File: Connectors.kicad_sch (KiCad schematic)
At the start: 18 parts, among them J1 Keystone 3579, J10 G-Switch-GT-USB-7025, J11 1.27mm 4 pin socket, J2 JST XH-S Balance Plug, J3 Keystone 3579, J4 Keystone 3569, J5 Keystone 3569, J6 Keystone 3579, J7 Keystone 3579, J8 Keystone 3569, J9 Keystone 3569

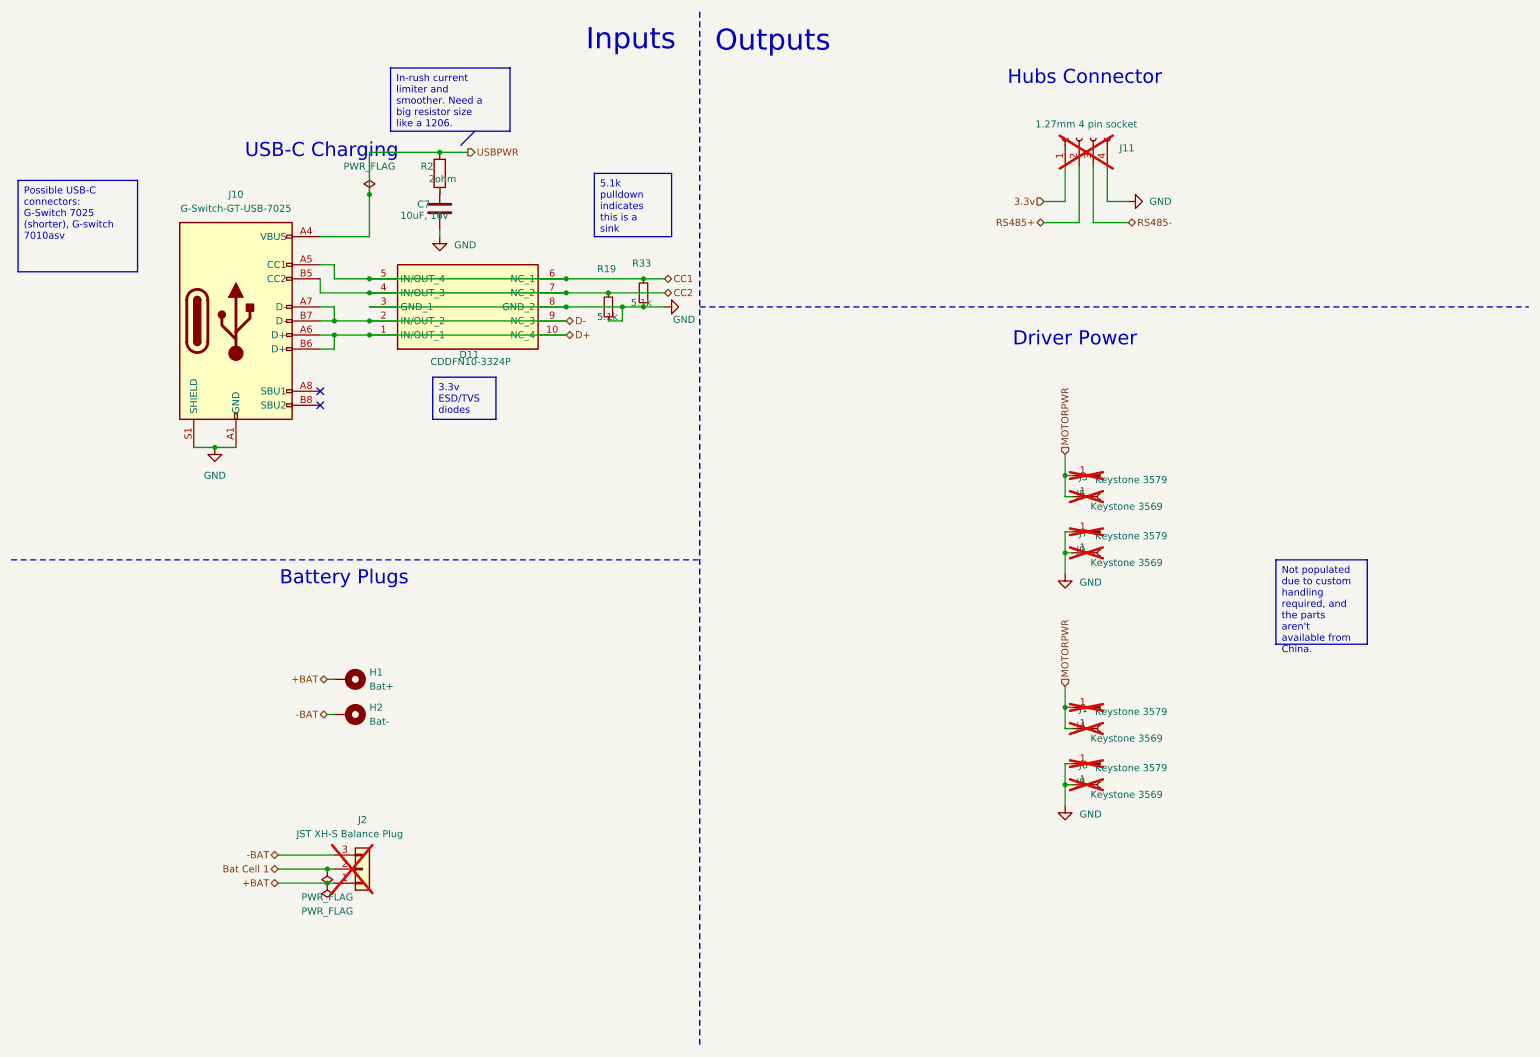
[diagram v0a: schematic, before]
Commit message: Updated to kicad 9
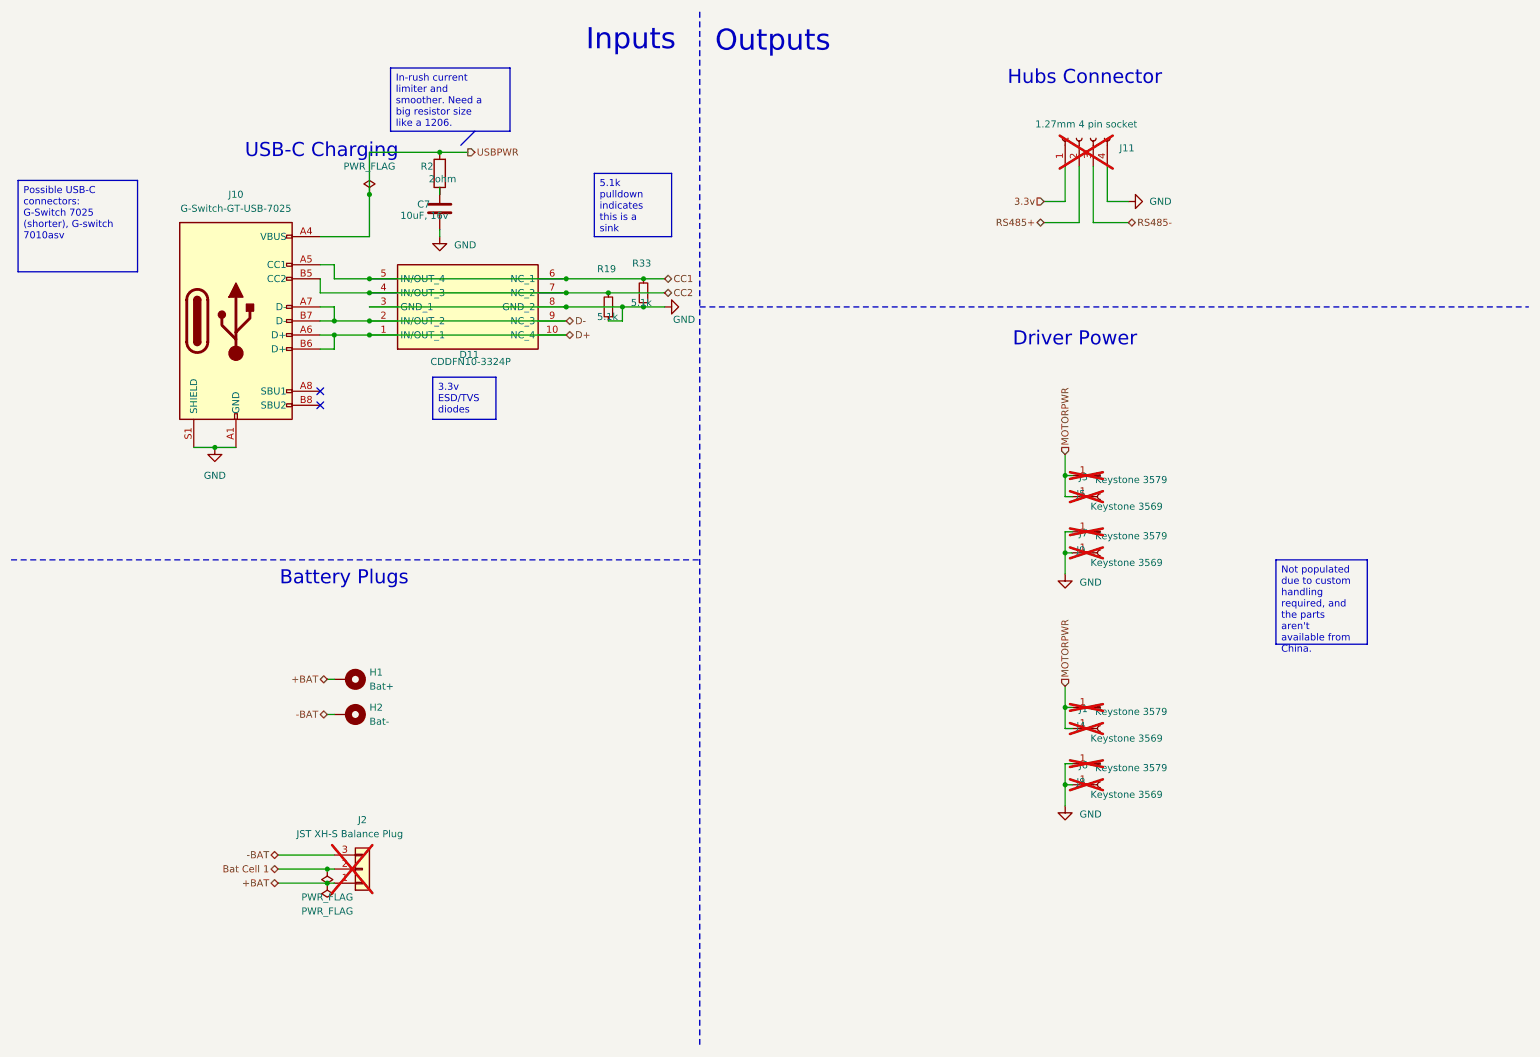
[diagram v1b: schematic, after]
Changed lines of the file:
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@@
 (kicad_sch
-	(version 20231120)
+	(version 20250114)
 	(generator "eeschema")
-	(generator_version "8.0")
+	(generator_version "9.0")
 	(paper "A4")
 	(title_block
 		(title "CACKLE 2s 40A PSU & Charger")
-		(date "2024-12-23")
-		(rev "V1")
+		(date "2025-11-17")
+		(rev "V1.1")
 		(company "Author: Asher Edwards")
 		(comment 1 "Licensed under CERN-OHL-S")
 	)
+	(text "Outputs"
+		(exclude_from_sim no)
+		(at 149.098 16.764 0)
+		(effects
+			(font
+				(size 3.81 3.81)
+			)
+		)
+	)
+	(text "USB-C Charging"
+		(exclude_from_sim no)
+		(at 67.564 36.576 0)
+		(effects
+			(font
+				(size 2.54 2.54)
+			)
+		)
+	)
+	(text "Inputs"
+		(exclude_from_sim no)
+		(at 123.444 16.51 0)
+		(effects
+			(font
+				(size 3.81 3.81)
+			)
+		)
+	)
+	(text "Driver Power"
+		(exclude_from_sim no)
+		(at 203.708 70.612 0)
+		(effects
+			(font
+				(size 2.54 2.54)
+			)
+		)
+	)
+	(text "Hubs Connector"
+		(exclude_from_sim no)
+		(at 205.486 23.368 0)
+		(effects
+			(font
+				(size 2.54 2.54)
+			)
+		)
+	)
+	(text "Battery Plugs"
+		(exclude_from_sim no)
+		(at 71.628 113.792 0)
+		(effects
+			(font
+				(size 2.54 2.54)
+			)
+		)
+	)
+	(text_box "In-rush current limiter and smoother. Need a big resistor size like a 1206."
+		(exclude_from_sim no)
+		(at 80.01 21.59 0)
+		(size 21.59 11.43)
+		(margins 0.9525 0.9525 0.9525 0.9525)
+		(stroke
+			(width 0)
+			(type default)
+		)
+		(fill
+			(type none)
+		)
+		(effects
+			(font
+				(size 1.27 1.27)
+			)
+			(justify left top)
+		)
+	)
+	(text_box "5.1k pulldown indicates this is a sink"
+		(exclude_from_sim no)
+		(at 116.84 40.64 0)
+		(size 13.97 11.43)
+		(margins 0.9525 0.9525 0.9525 0.9525)
+		(stroke
+			(width 0)
+			(type default)
+		)
+		(fill
+			(type none)
+		)
+		(effects
+			(font
+				(size 1.27 1.27)
+			)
+			(justify left top)
+		)
+	)
+	(text_box "Possible USB-C connectors: G-Switch 7025 (shorter), G-switch 7010asv"
+		(exclude_from_sim no)
+		(at 12.7 41.91 0)
+		(size 21.59 16.51)
+		(margins 0.9525 0.9525 0.9525 0.9525)
+		(stroke
+			(width 0)
+			(type default)
+		)
+		(fill
+			(type none)
+		)
+		(effects
+			(font
+				(size 1.27 1.27)
+			)
+			(justify left top)
+		)
+	)
+	(text_box "3.3v ESD/TVS diodes"
+		(exclude_from_sim no)
+		(at 87.63 77.47 0)
+		(size 11.43 7.62)
+		(margins 0.9525 0.9525 0.9525 0.9525)
+		(stroke
+			(width 0)
+			(type default)
+		)
+		(fill
+			(type none)
+		)
+		(effects
+			(font
+				(size 1.27 1.27)
+			)
+			(justify left top)
+		)
+	)
+	(text_box "Not populated due to custom handling required, and the parts aren't available from China."
+		(exclude_from_sim no)
+		(at 240.03 110.49 0)
+		(size 16.51 15.24)
+		(margins 0.9525 0.9525 0.9525 0.9525)
+		(stroke
+			(width 0)
+			(type default)
+		)
+		(fill
+			(type none)
+		)
+		(effects
+			(font
+				(size 1.27 1.27)
+			)
+			(justify left top)
+		)
+	)
 	(junction
 		(at 76.2 69.85)
@@
 		)
 	)
-	(text_box "In-rush current limiter and smoother. Need a big resistor size like a 1206."
-		(exclude_from_sim no)
-		(at 80.01 21.59 0)
-		(size 21.59 11.43)
-		(stroke
-			(width 0)
-			(type default)
-		)
-		(fill
-			(type none)
-		)
-		(effects
-			(font
-				(size 1.27 1.27)
-			)
-			(justify left top)
-		)
-	)
-	(text_box "5.1k pulldown indicates this is a sink"
-		(exclude_from_sim no)
-		(at 116.84 40.64 0)
-		(size 13.97 11.43)
-		(stroke
-			(width 0)
-			(type default)
-		)
-		(fill
-			(type none)
-		)
-		(effects
-			(font
-				(size 1.27 1.27)
-			)
-			(justify left top)
-		)
-	)
-	(text_box "Possible USB-C connectors: G-Switch 7025 (shorter), G-switch 7010asv"
-		(exclude_from_sim no)
-		(at 12.7 41.91 0)
-		(size 21.59 16.51)
-		(stroke
-			(width 0)
-			(type default)
-		)
-		(fill
-			(type none)
-		)
-		(effects
-			(font
-				(size 1.27 1.27)
-			)
-			(justify left top)
-		)
-	)
-	(text_box "3.3v ESD/TVS diodes"
-		(exclude_from_sim no)
-		(at 87.63 77.47 0)
-		(size 11.43 7.62)
-		(stroke
-			(width 0)
-			(type default)
-		)
-		(fill
-			(type none)
-		)
-		(effects
-			(font
-				(size 1.27 1.27)
-			)
-			(justify left top)
-		)
-	)
-	(text_box "Not populated due to custom handling required, and the parts aren't available from China."
-		(exclude_from_sim no)
-		(at 240.03 110.49 0)
-		(size 16.51 15.24)
-		(stroke
-			(width 0)
-			(type default)
-		)
-		(fill
-			(type none)
-		)
-		(effects
-			(font
-				(size 1.27 1.27)
-			)
-			(justify left top)
-		)
-	)
-	(text "Outputs"
-		(exclude_from_sim no)
-		(at 149.098 16.764 0)
-		(effects
-			(font
-				(size 3.81 3.81)
-			)
-		)
-	)
-	(text "USB-C Charging"
-		(exclude_from_sim no)
-		(at 67.564 36.576 0)
-		(effects
-			(font
-				(size 2.54 2.54)
-			)
-		)
-	)
-	(text "Inputs"
-		(exclude_from_sim no)
-		(at 123.444 16.51 0)
-		(effects
-			(font
-				(size 3.81 3.81)
-			)
-		)
-	)
-	(text "Driver Power"
-		(exclude_from_sim no)
-		(at 203.708 70.612 0)
-		(effects
-			(font
-				(size 2.54 2.54)
-			)
-		)
-	)
-	(text "Hubs Connector"
-		(exclude_from_sim no)
-		(at 205.486 23.368 0)
-		(effects
-			(font
-				(size 2.54 2.54)
-			)
-		)
-	)
-	(text "Battery Plugs"
-		(exclude_from_sim no)
-		(at 71.628 113.792 0)
-		(effects
-			(font
-				(size 2.54 2.54)
-			)
-		)
-	)
 	(hierarchical_label "RS485+"
 		(shape bidirectional)
 		(at 198.12 49.53 180)
-		(fields_autoplaced yes)
 		(effects
 			(font
@@
 		(shape bidirectional)
 		(at 129.54 59.69 0)
-		(fields_autoplaced yes)
 		(effects
 			(font
@@
 		(shape bidirectional)
 		(at 129.54 62.23 0)
-		(fields_autoplaced yes)
 		(effects
 			(font
@@
 		(shape bidirectional)
 		(at 111.76 67.31 0)
-		(fields_autoplaced yes)
 		(effects
 			(font
@@
 		(shape bidirectional)
 		(at 111.76 69.85 0)
-		(fields_autoplaced yes)
 		(effects
 			(font
@@
 		(shape bidirectional)
 		(at 213.36 49.53 0)
-		(fields_autoplaced yes)
 		(effects
 			(font
@@
 		)
 	)
+	(embedded_fonts no)
 )

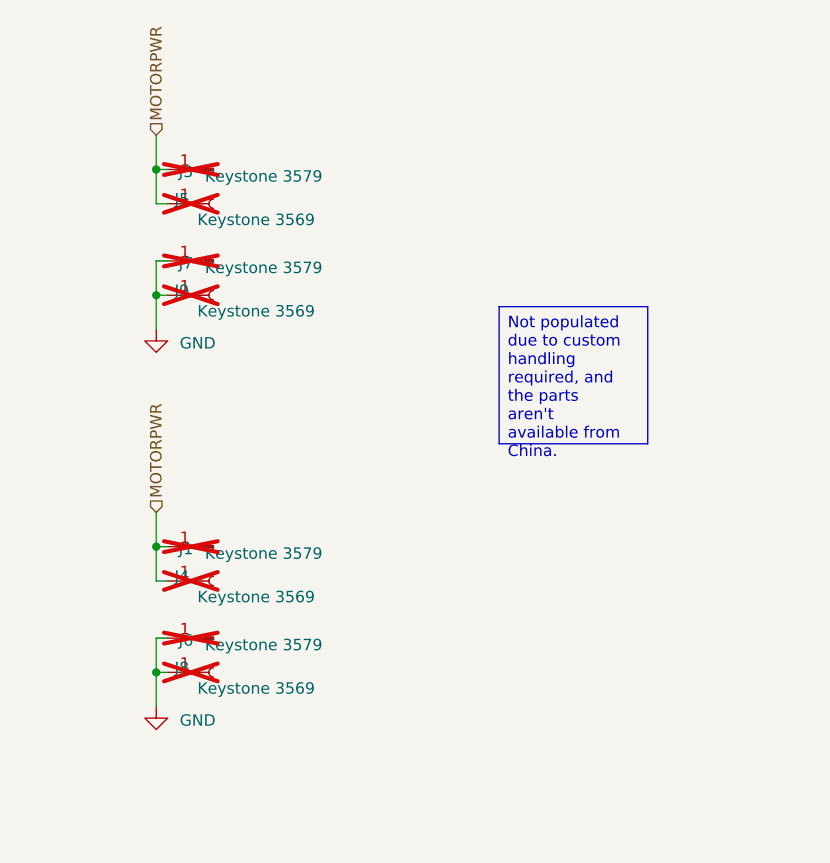
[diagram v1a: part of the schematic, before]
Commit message: Updated power connectors
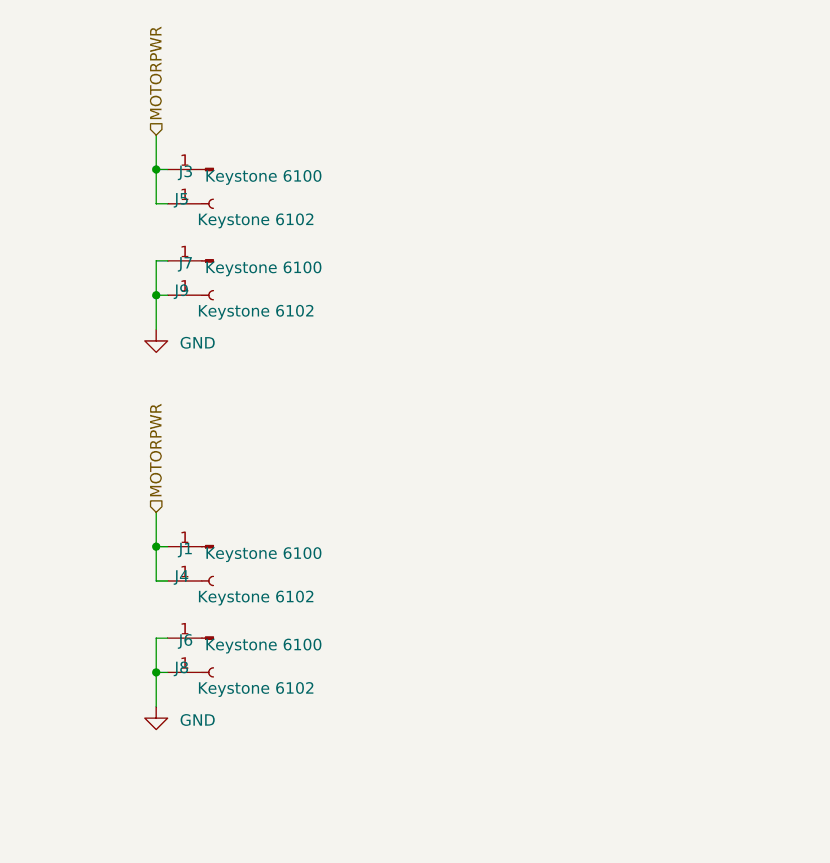
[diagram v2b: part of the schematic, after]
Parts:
- J1, J3, J6, J7: value Keystone 3579 -> Keystone 6100; footprint custom_Connector:Keystone_3579 -> custom_Connector:Keystone_6100; now fitted
- J4, J5, J8, J9: value Keystone 3569 -> Keystone 6102; footprint custom_Connector:Keystone_3569_half -> custom_Connector:Keystone_6102; now fitted
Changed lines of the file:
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@@
-		)
-	)
-	(text_box "Not populated due to custom handling required, and the parts aren't available from China."
-		(exclude_from_sim no)
-		(at 240.03 110.49 0)
-		(size 16.51 15.24)
-		(margins 0.9525 0.9525 0.9525 0.9525)
-		(stroke
-			(width 0)
-			(type default)
-		)
-		(fill
-			(type none)
-		)
-		(effects
-			(font
-				(size 1.27 1.27)
-			)
-			(justify left top)
 		)
 	)
@@
 		(in_bom yes)
 		(on_board yes)
-		(dnp yes)
+		(dnp no)
 		(property "Reference" "J4"
 			(at 203.962 140.462 0)
@@
 			)
 		)
-		(property "Value" "Keystone 3569"
+		(property "Value" "Keystone 6102"
 			(at 206.502 142.748 0)
 			(effects
@@
 			)
 		)
-		(property "Footprint" "custom_Connector:Keystone_3569_half"
+		(property "Footprint" "custom_Connector:Keystone_6102"
 			(at 208.28 140.97 0)
 			(effects
@@
 		(in_bom yes)
 		(on_board yes)
-		(dnp yes)
+		(dnp no)
 		(property "Reference" "J7"
 			(at 205.232 105.664 0)
@@
 			)
 		)
-		(property "Value" "Keystone 3579"
+		(property "Value" "Keystone 6100"
 			(at 213.868 106.172 0)
 			(effects
@@
 			)
 		)
-		(property "Footprint" "custom_Connector:Keystone_3579"
+		(property "Footprint" "custom_Connector:Keystone_6100"
 			(at 208.28 105.41 0)
 			(effects
@@
 		(in_bom yes)
 		(on_board yes)
-		(dnp yes)
+		(dnp no)
 		(property "Reference" "J3"
 			(at 205.232 95.504 0)
@@
 			)
 		)
-		(property "Value" "Keystone 3579"
+		(property "Value" "Keystone 6100"
 			(at 213.868 96.012 0)
 			(effects
@@
 			)
 		)
-		(property "Footprint" "custom_Connector:Keystone_3579"
+		(property "Footprint" "custom_Connector:Keystone_6100"
 			(at 208.28 95.25 0)
 			(effects
@@
 		(in_bom yes)
 		(on_board yes)
-		(dnp yes)
+		(dnp no)
 		(property "Reference" "J1"
 			(at 205.232 137.414 0)
@@
 			)
 		)
-		(property "Value" "Keystone 3579"
+		(property "Value" "Keystone 6100"
 			(at 213.868 137.922 0)
 			(effects
@@
 			)
 		)
-		(property "Footprint" "custom_Connector:Keystone_3579"
+		(property "Footprint" "custom_Connector:Keystone_6100"
 			(at 208.28 137.16 0)
 			(effects
@@
 		(in_bom yes)
 		(on_board yes)
-		(dnp yes)
+		(dnp no)
 		(property "Reference" "J8"
 			(at 203.962 150.622 0)
@@
 			)
 		)
-		(property "Value" "Keystone 3569"
+		(property "Value" "Keystone 6102"
 			(at 206.502 152.908 0)
 			(effects
@@
 			)
 		)
-		(property "Footprint" "custom_Connector:Keystone_3569_half"
+		(property "Footprint" "custom_Connector:Keystone_6102"
 			(at 208.28 151.13 0)
 			(effects
@@
 		(in_bom yes)
 		(on_board yes)
-		(dnp yes)
+		(dnp no)
 		(property "Reference" "J5"
 			(at 203.962 98.552 0)
@@
 			)
 		)
-		(property "Value" "Keystone 3569"
+		(property "Value" "Keystone 6102"
 			(at 206.502 100.838 0)
 			(effects
@@
 			)
 		)
-		(property "Footprint" "custom_Connector:Keystone_3569_half"
+		(property "Footprint" "custom_Connector:Keystone_6102"
 			(at 208.28 99.06 0)
 			(effects
@@
 		(in_bom yes)
 		(on_board yes)
-		(dnp yes)
+		(dnp no)
 		(property "Reference" "J9"
 			(at 203.962 108.712 0)
@@
 			)
 		)
-		(property "Value" "Keystone 3569"
+		(property "Value" "Keystone 6102"
 			(at 206.502 110.998 0)
 			(effects
@@
 			)
 		)
-		(property "Footprint" "custom_Connector:Keystone_3569_half"
+		(property "Footprint" "custom_Connector:Keystone_6102"
 			(at 208.28 109.22 0)
 			(effects
@@
 		(in_bom yes)
 		(on_board yes)
-		(dnp yes)
+		(dnp no)
 		(property "Reference" "J6"
 			(at 205.232 147.574 0)
@@
 			)
 		)
-		(property "Value" "Keystone 3579"
+		(property "Value" "Keystone 6100"
 			(at 213.868 148.082 0)
 			(effects
@@
 			)
 		)
-		(property "Footprint" "custom_Connector:Keystone_3579"
+		(property "Footprint" "custom_Connector:Keystone_6100"
 			(at 208.28 147.32 0)
 			(effects

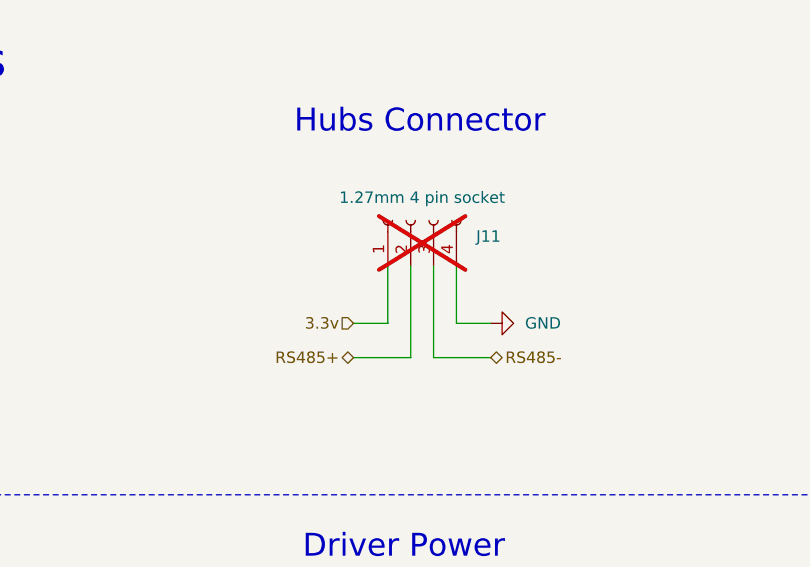
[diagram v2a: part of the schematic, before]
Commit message: Corrected hub connector
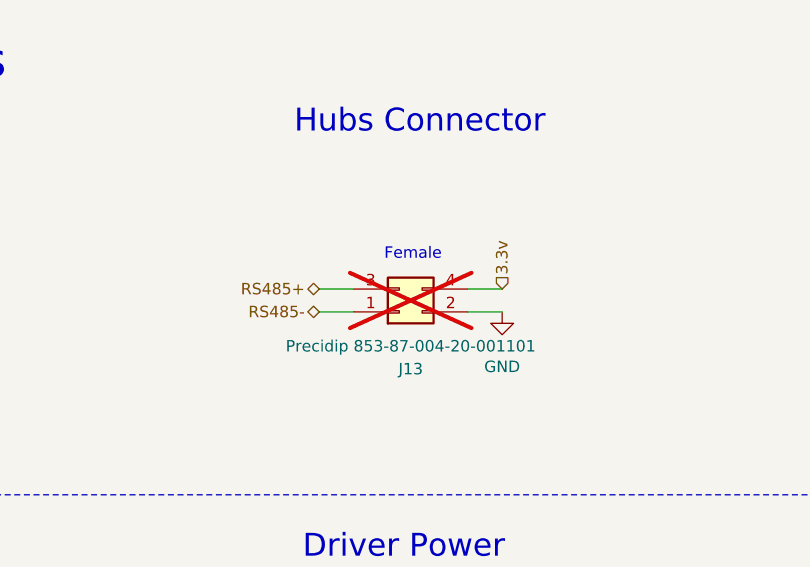
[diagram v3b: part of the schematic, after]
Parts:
- removed J11: 1.27mm 4 pin socket, Connector_PinSocket_1.27mm:PinSocket_1x04_P1.27mm_Vertical, symbol Connector:Conn_01x04_Socket
- added J13: Precidip 853-87-004-20-001101, custom_Connector:Precidip 853-87-004-20-001101, symbol Connector_Generic:Conn_02x02_Odd_Even
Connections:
- net 3.3v: now also J13.4 (Pin_4)
- net GND: now also J13.2 (Pin_2)
- net RS485+: now also J13.3 (Pin_3)
- net RS485-: now also J13.1 (Pin_1)
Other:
- note added: "Female"
